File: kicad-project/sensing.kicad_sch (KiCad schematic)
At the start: 11 parts, among them J11 Panel+ Connector, J8 Panel- Connector

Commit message: hw: final changes
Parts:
- R23: value R -> (none)
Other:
- note added: "Second resistor is in case we want to increase the sensitivity"
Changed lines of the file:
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@@
+    (effects (font (size 1.27 1.27)) (justify left bottom))
+  )
+  (text "Second resistor is in case we want to increase the sensitivity"
+    (at 99.06 73.66 0)
     (effects (font (size 1.27 1.27)) (justify left bottom))
   )
@@
       (effects (font (size 1.27 1.27)) (justify left))
     )
-    (property "Value" "R" (id 1) (at 116.84 58.4199 0)
+    (property "Value" "" (id 1) (at 116.84 58.4199 0)
       (effects (font (size 1.27 1.27)) (justify left))
     )

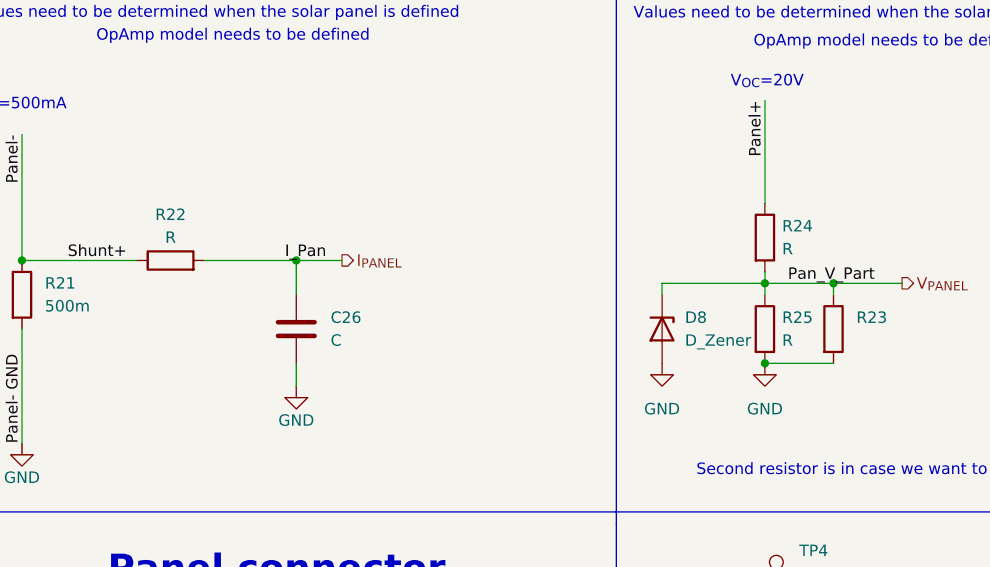
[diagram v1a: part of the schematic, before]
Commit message: hw: add sensing resistance values
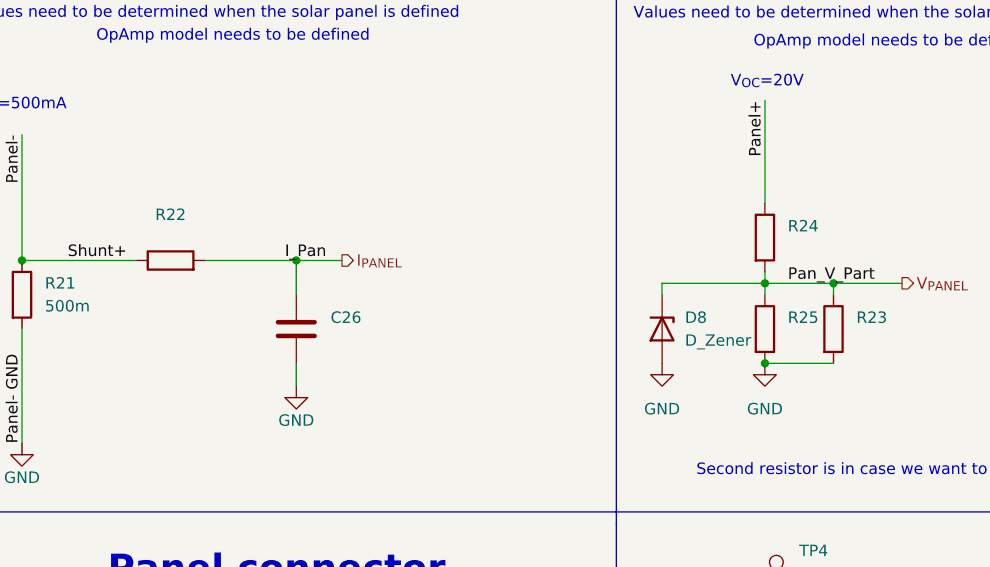
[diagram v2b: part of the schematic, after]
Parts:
- C26: value C -> (none)
- R22, R24, R25: value R -> (none)
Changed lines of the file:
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@@
   (symbol (lib_id "Device:R") (at 106.68 57.15 0) (unit 1)
     (in_bom yes) (on_board yes) (fields_autoplaced)
-    (property "Reference" "R25" (id 0) (at 108.585 55.8799 0)
+    (property "Reference" "R25" (id 0) (at 109.22 55.8799 0)
       (effects (font (size 1.27 1.27)) (justify left))
     )
-    (property "Value" "R" (id 1) (at 108.585 58.4199 0)
+    (property "Value" "" (id 1) (at 109.22 58.4199 0)
       (effects (font (size 1.27 1.27)) (justify left))
     )
@@
   (symbol (lib_id "Device:R") (at 106.68 46.99 0) (unit 1)
     (in_bom yes) (on_board yes) (fields_autoplaced)
-    (property "Reference" "R24" (id 0) (at 108.585 45.7199 0)
+    (property "Reference" "R24" (id 0) (at 109.22 45.7199 0)
       (effects (font (size 1.27 1.27)) (justify left))
     )
-    (property "Value" "R" (id 1) (at 108.585 48.2599 0)
+    (property "Value" "" (id 1) (at 109.22 48.2599 0)
       (effects (font (size 1.27 1.27)) (justify left))
     )
@@
       (effects (font (size 1.27 1.27)) (justify left))
     )
-    (property "Value" "C" (id 1) (at 58.42 58.4199 0)
+    (property "Value" "" (id 1) (at 58.42 58.4199 0)
       (effects (font (size 1.27 1.27)) (justify left))
     )
@@
     (in_bom yes) (on_board yes)
     (property "Reference" "R22" (id 0) (at 40.64 44.45 90))
-    (property "Value" "R" (id 1) (at 40.64 46.99 90))
+    (property "Value" "" (id 1) (at 40.64 46.99 90))
     (property "Footprint" "Resistor_SMD:R_0603_1608Metric" (id 2) (at 40.64 51.308 90)
       (effects (font (size 1.27 1.27)) hide)

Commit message: hw: schematic updates
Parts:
- C26: value (none) -> 100n
- R22: value (none) -> 10k
- R23: value (none) -> 4k7 DNP
- R24: value (none) -> 33k
- R25: value (none) -> 4k7
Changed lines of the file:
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@@
       (effects (font (size 1.27 1.27)) (justify left))
     )
-    (property "Value" "" (id 1) (at 109.22 58.4199 0)
+    (property "Value" "4k7" (id 1) (at 109.22 58.4199 0)
       (effects (font (size 1.27 1.27)) (justify left))
     )
@@
       (effects (font (size 1.27 1.27)) (justify left))
     )
-    (property "Value" "" (id 1) (at 116.84 58.4199 0)
+    (property "Value" "4k7 DNP" (id 1) (at 116.84 58.4199 0)
       (effects (font (size 1.27 1.27)) (justify left))
     )
@@
       (effects (font (size 1.27 1.27)) (justify left))
     )
-    (property "Value" "" (id 1) (at 109.22 48.2599 0)
+    (property "Value" "33k" (id 1) (at 109.22 48.2599 0)
       (effects (font (size 1.27 1.27)) (justify left))
     )
@@
       (effects (font (size 1.27 1.27)) (justify left))
     )
-    (property "Value" "" (id 1) (at 58.42 58.4199 0)
+    (property "Value" "100n" (id 1) (at 58.42 58.4199 0)
       (effects (font (size 1.27 1.27)) (justify left))
     )
@@
     (in_bom yes) (on_board yes)
     (property "Reference" "R22" (id 0) (at 40.64 44.45 90))
-    (property "Value" "" (id 1) (at 40.64 46.99 90))
+    (property "Value" "10k" (id 1) (at 40.64 46.99 90))
     (property "Footprint" "Resistor_SMD:R_0603_1608Metric" (id 2) (at 40.64 51.308 90)
       (effects (font (size 1.27 1.27)) hide)

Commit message: hw: changes for the simia
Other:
- note added: "Ground connection"
- note added: "Negative pole of panel"
- note added: "Second resistor is in case we want to increase the input range"
- note removed: "Depending on panel power, might need more suitable connector"
- note removed: "OpAmp model needs to be defined"
- note removed: "Second resistor is in case we want to increase the sensitivity"
- note removed: "Values need to be determined when the solar panel is defined"
- moved on the sheet: C26, D8, R21, R22, R23, R24, R25

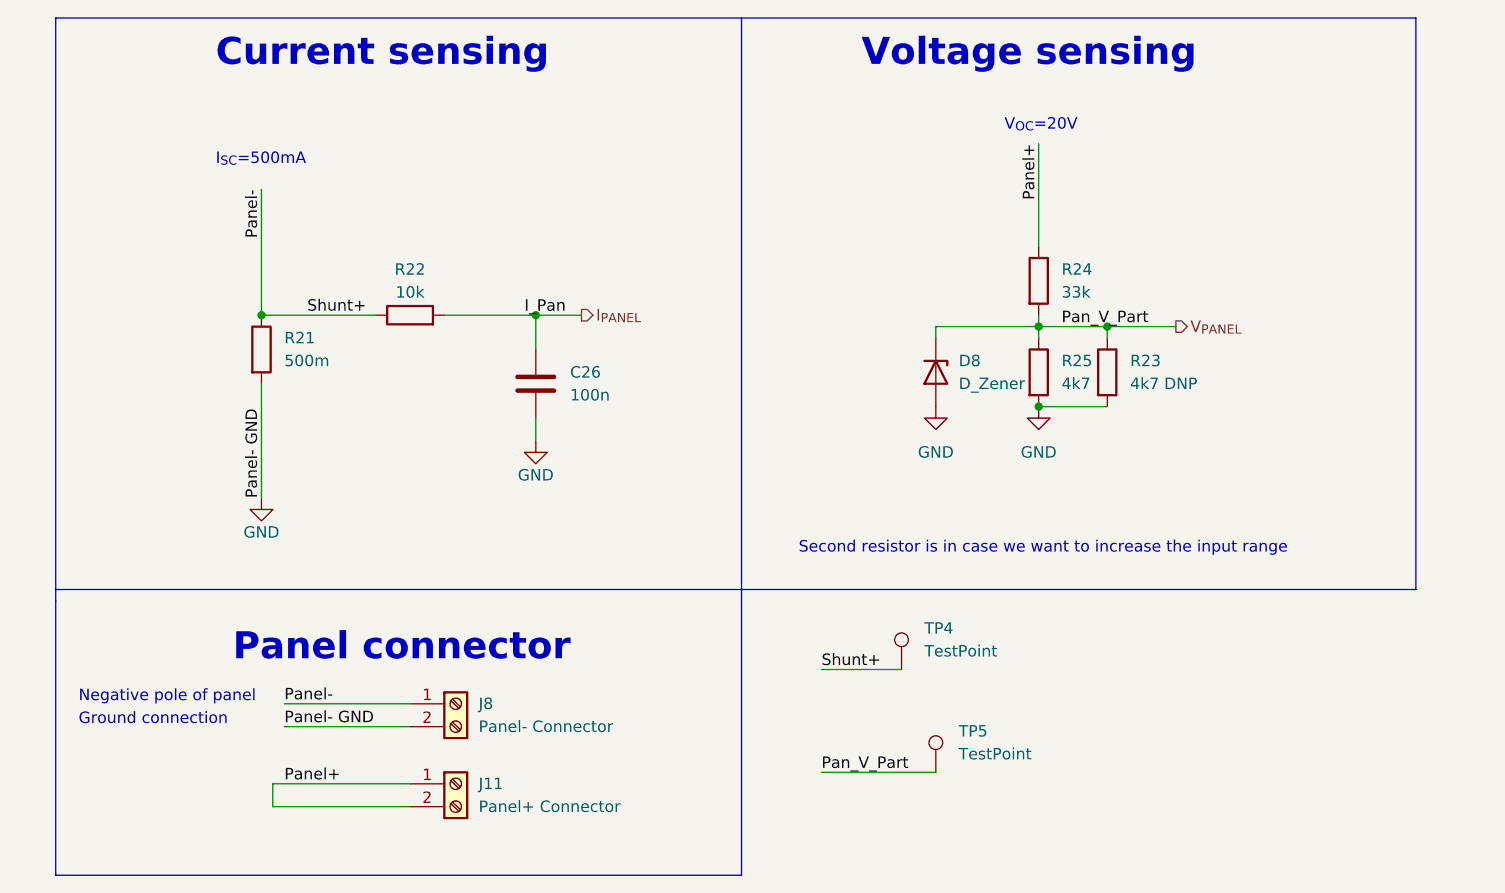
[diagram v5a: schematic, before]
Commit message: hw: change some small notes
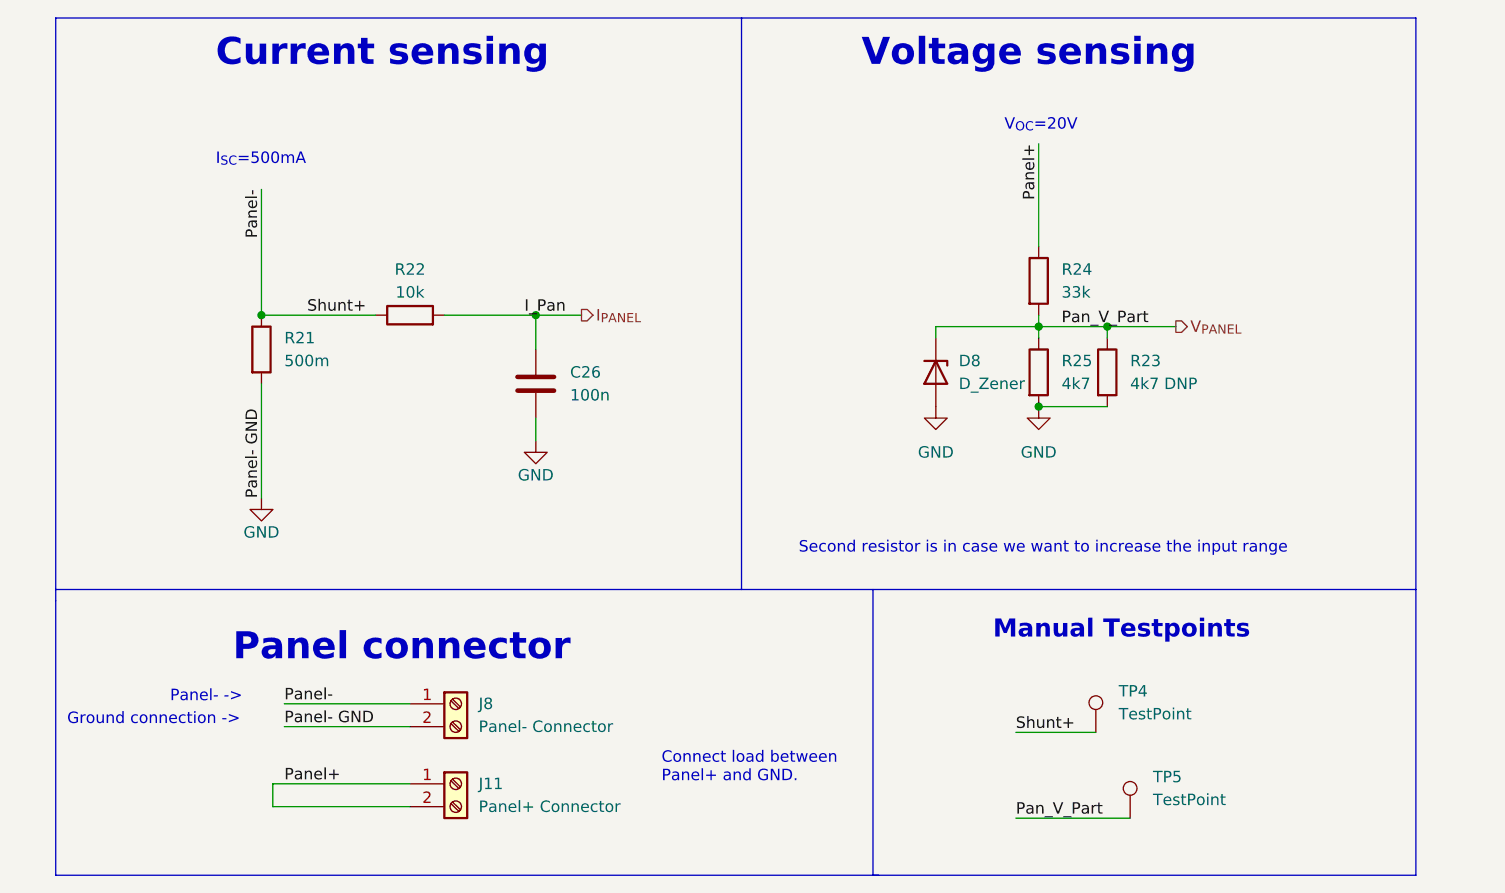
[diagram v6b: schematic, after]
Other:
- note added: "Connect load between Panel+ and GND."
- note added: "Ground connection ->"
- note added: "Manual Testpoints"
- note added: "Panel- ->"
- note removed: "Ground connection"
- note removed: "Negative pole of panel"
- moved on the sheet: TP4, TP5
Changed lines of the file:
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@@
     (stroke (width 0) (type default) (color 0 0 0 0))
   )
-  (polyline (pts (xy 90.17 109.22) (xy 90.17 78.74))
-    (stroke (width 0) (type default) (color 0 0 0 0))
-  )
-  (polyline (pts (xy 90.17 78.74) (xy 90.17 13.97))
+  (polyline (pts (xy 90.17 77.47) (xy 90.17 13.97))
     (stroke (width 0) (type default) (color 0 0 0 0))
   )
@@
     (stroke (width 0) (type default) (color 0 0 0 0))
   )
+  (polyline (pts (xy 104.775 77.47) (xy 104.775 109.22))
+    (stroke (width 0) (type default) (color 0 0 0 0))
+  )
   (wire (pts (xy 53.34 90.17) (xy 39.37 90.17))
     (stroke (width 0) (type default) (color 0 0 0 0))
@@
     (stroke (width 0) (type default) (color 0 0 0 0))
   )
-  (polyline (pts (xy 13.97 109.22) (xy 90.17 109.22))
+  (polyline (pts (xy 13.97 109.22) (xy 105.41 109.22))
+    (stroke (width 0) (type default) (color 0 0 0 0))
+  )
+  (polyline (pts (xy 165.1 109.22) (xy 165.1 77.47))
     (stroke (width 0) (type default) (color 0 0 0 0))
   )
@@
     (stroke (width 0) (type default) (color 0 0 0 0))
   )
-  (wire (pts (xy 99.06 97.79) (xy 111.76 97.79))
+  (wire (pts (xy 120.65 102.87) (xy 133.35 102.87))
     (stroke (width 0) (type default) (color 0 0 0 0))
   )
@@
     (stroke (width 0) (type default) (color 0 0 0 0))
   )
-  (wire (pts (xy 99.06 86.36) (xy 107.95 86.36))
+  (wire (pts (xy 120.65 93.345) (xy 129.54 93.345))
     (stroke (width 0) (type default) (color 0 0 0 0))
   )
   (wire (pts (xy 36.83 54.61) (xy 36.83 67.31))
+    (stroke (width 0) (type default) (color 0 0 0 0))
+  )
+  (polyline (pts (xy 104.775 109.22) (xy 165.1 109.22))
     (stroke (width 0) (type default) (color 0 0 0 0))
   )
@@
     (effects (font (size 1.27 1.27)) (justify left bottom))
   )
+  (text "Connect load between\nPanel+ and GND." (at 81.28 99.06 0)
+    (effects (font (size 1.27 1.27)) (justify left bottom))
+  )
   (text "Panel connector" (at 33.655 85.725 0)
     (effects (font (size 3 3) (thickness 0.6) bold) (justify left bottom))
   )
-  (text "Negative pole of panel" (at 16.51 90.17 0)
-    (effects (font (size 1.27 1.27)) (justify left bottom))
-  )
-  (text "Ground connection" (at 16.51 92.71 0)
-    (effects (font (size 1.27 1.27)) (justify left bottom))
+  (text "Panel- ->" (at 26.67 90.17 0)
+    (effects (font (size 1.27 1.27)) (justify left bottom))
+  )
+  (text "Ground connection ->" (at 15.24 92.71 0)
+    (effects (font (size 1.27 1.27)) (justify left bottom))
+  )
+  (text "Manual Testpoints" (at 118.11 83.185 0)
+    (effects (font (size 2 2) (thickness 0.4) bold) (justify left bottom))
   )
   (label "Panel- GND" (at 36.83 67.31 90)
@@
     (effects (font (size 1.27 1.27)) (justify left bottom))
   )
-  (label "Shunt+" (at 99.06 86.36 0)
+  (label "Shunt+" (at 120.65 93.345 0)
     (effects (font (size 1.27 1.27)) (justify left bottom))
   )
@@
     (effects (font (size 1.27 1.27)) (justify left bottom))
   )
-  (label "Pan_V_Part" (at 99.06 97.79 0)
+  (label "Pan_V_Part" (at 120.65 102.87 0)
     (effects (font (size 1.27 1.27)) (justify left bottom))
   )
@@
     (pin "2")
   )
-  (symbol (lib_id "Connector:TestPoint") (at 107.95 86.36 0) (unit 1)
-    (in_bom yes) (on_board yes) (fields_autoplaced)
-    (property "Reference" "TP4" (id 0) (at 110.49 81.7879 0)
-      (effects (font (size 1.27 1.27)) (justify left))
-    )
-    (property "Value" "TestPoint" (id 1) (at 110.49 84.3279 0)
-      (effects (font (size 1.27 1.27)) (justify left))
-    )
-    (property "Footprint" "TestPoint:TestPoint_Keystone_5005-5009_Compact" (id 2) (at 113.03 86.36 0)
-      (effects (font (size 1.27 1.27)) hide)
-    )
-    (property "Datasheet" "~" (id 3) (at 113.03 86.36 0)
-      (effects (font (size 1.27 1.27)) hide)
-    )
-    (pin "1")
-  )
-  (symbol (lib_id "Connector:TestPoint") (at 111.76 97.79 0) (unit 1)
-    (in_bom yes) (on_board yes) (fields_autoplaced)
-    (property "Reference" "TP5" (id 0) (at 114.3 93.2179 0)
-      (effects (font (size 1.27 1.27)) (justify left))
-    )
-    (property "Value" "TestPoint" (id 1) (at 114.3 95.7579 0)
-      (effects (font (size 1.27 1.27)) (justify left))
-    )
-    (property "Footprint" "TestPoint:TestPoint_Keystone_5005-5009_Compact" (id 2) (at 116.84 97.79 0)
-      (effects (font (size 1.27 1.27)) hide)
-    )
-    (property "Datasheet" "~" (id 3) (at 116.84 97.79 0)
-      (effects (font (size 1.27 1.27)) hide)
-    )
+  (symbol (lib_id "Connector:TestPoint") (at 129.54 93.345 0) (unit 1)
+    (in_bom yes) (on_board yes) (fields_autoplaced)
+    (property "Reference" "TP4" (id 0) (at 132.08 88.7729 0)
+      (effects (font (size 1.27 1.27)) (justify left))
+    )
+    (property "Value" "TestPoint" (id 1) (at 132.08 91.3129 0)
+      (effects (font (size 1.27 1.27)) (justify left))
+    )
+    (property "Footprint" "TestPoint:TestPoint_Keystone_5005-5009_Compact" (id 2) (at 134.62 93.345 0)
+      (effects (font (size 1.27 1.27)) hide)
+    )
+    (property "Datasheet" "~" (id 3) (at 134.62 93.345 0)
+      (effects (font (size 1.27 1.27)) hide)
+    )
+    (pin "1")
+  )
+  (symbol (lib_id "Connector:TestPoint") (at 133.35 102.87 0) (unit 1)
+    (in_bom yes) (on_board yes) (fields_autoplaced)
+    (property "Reference" "TP5" (id 0) (at 135.89 98.2979 0)
+      (effects (font (size 1.27 1.27)) (justify left))
+    )
+    (property "Value" "TestPoint" (id 1) (at 135.89 100.8379 0)
+      (effects (font (size 1.27 1.27)) (justify left))
+    )
+    (property "Footprint" "TestPoint:TestPoint_Keystone_5005-5009_Compact" (id 2) (at 138.43 102.87 0)
+      (effects (font (size 1.27 1.27)) hide)
+    )
+    (property "Datasheet" "~" (id 3) (at 138.43 102.87 0)
+      (effects (font (size 1.27 1.27)) hide)
+    )
